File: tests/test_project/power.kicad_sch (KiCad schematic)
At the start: 19 parts, among them J3 Barrel_Jack_MountingPin, U3 LM3880, U4 AP2112K-1.8, U6 RT9742AGJ5F

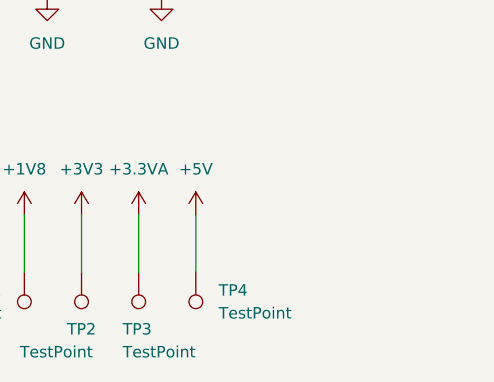
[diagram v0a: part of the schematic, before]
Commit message: [#68432] Add design errors to PCB
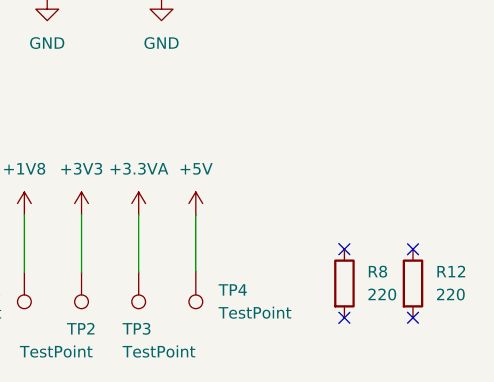
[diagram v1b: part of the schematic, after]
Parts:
- added R12, R8: 220, Resistor_SMD:R_0402_1005Metric, symbol Device:R
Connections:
- no-connect marks 1 -> 5
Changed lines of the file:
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@@
+	)
+	(no_connect
+		(at 265.43 147.32)
+	)
+	(no_connect
+		(at 273.05 147.32)
 	)
 	(no_connect
 		(at 127 116.84)
+	)
+	(no_connect
+		(at 273.05 139.7)
+	)
+	(no_connect
+		(at 265.43 139.7)
 	)
 	(wire
@@
 	)
 	(symbol
+		(lib_id "Device:R")
+		(at 273.05 143.51 0)
+		(unit 1)
+		(exclude_from_sim no)
+		(in_bom yes)
+		(on_board yes)
+		(dnp no)
+		(fields_autoplaced yes)
+		(property "Reference" "R12"
+			(at 275.59 142.2399 0)
+			(effects
+				(font
+					(size 1.27 1.27)
+				)
+				(justify left)
+			)
+		)
+		(property "Value" "220"
+			(at 275.59 144.7799 0)
+			(effects
+				(font
+					(size 1.27 1.27)
+				)
+				(justify left)
+			)
+		)
+		(property "Footprint" "Resistor_SMD:R_0402_1005Metric"
+			(at 271.272 143.51 90)
+			(effects
+				(font
+					(size 1.27 1.27)
+				)
+				(hide yes)
+			)
+		)
+		(property "Datasheet" "~"
+			(at 273.05 143.51 0)
+			(effects
+				(font
+					(size 1.27 1.27)
+				)
+				(hide yes)
+			)
+		)
+		(property "Description" "Resistor"
+			(at 273.05 143.51 0)
+			(effects
+				(font
+					(size 1.27 1.27)
+				)
+				(hide yes)
+			)
+		)
+		(pin "1"
+		)
+		(pin "2"
+		)
+		(instances
+			(project "test_project"
+				(path "/59f522e0-0cf7-48a6-bc09-47b340553d24/9fb9e3b9-702c-4bf6-8780-47a0645875b6"
+					(reference "R12")
+					(unit 1)
+				)
+			)
+		)
+	)
+	(symbol
 		(lib_id "power:+3V3")
 		(at 74.93 102.87 0)
@@
 					(unit 1)
 				)
+			)
+		)
+	)
+	(symbol
+		(lib_id "Device:R")
+		(at 265.43 143.51 0)
+		(unit 1)
+		(exclude_from_sim no)
+		(in_bom yes)
+		(on_board yes)
+		(dnp no)
+		(fields_autoplaced yes)
+		(property "Reference" "R8"
+			(at 267.97 142.2399 0)
+			(effects
+				(font
+					(size 1.27 1.27)
+				)
+				(justify left)
+			)
+		)
+		(property "Value" "220"
+			(at 267.97 144.7799 0)
+			(effects
+				(font
+					(size 1.27 1.27)
+				)
+				(justify left)
+			)
+		)
+		(property "Footprint" "Resistor_SMD:R_0402_1005Metric"
+			(at 263.652 143.51 90)
+			(effects
+				(font
+					(size 1.27 1.27)
+				)
+				(hide yes)
+			)
+		)
+		(property "Datasheet" "~"
+			(at 265.43 143.51 0)
+			(effects
+				(font
+					(size 1.27 1.27)
+				)
+				(hide yes)
+			)
+		)
+		(property "Description" "Resistor"
+			(at 265.43 143.51 0)
+			(effects
+				(font
+					(size 1.27 1.27)
+				)
+				(hide yes)
+			)
+		)
+		(pin "1"
+		)
+		(pin "2"
+		)
+		(instances
+			(project "test_project"
+				(path "/59f522e0-0cf7-48a6-bc09-47b340553d24/9fb9e3b9-702c-4bf6-8780-47a0645875b6"
+					(reference "R8")
+					(unit 1)
+				)

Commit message: [#75441] Kicad9
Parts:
- R8: TODO (none) -> ${ERC_ERROR TODO}Manual ERC error (sym field)
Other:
- note added: "${ERC_WARNING "TODO Fill Table"} Manual ERC warning"
